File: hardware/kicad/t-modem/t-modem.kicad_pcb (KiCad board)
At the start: 2 copper layers, 190 x 110 mm, 43 parts, among them Q1 2N2222A, SW1 BOOTSEL, U1 RaspberryPi_Pico, Y1 4.433619

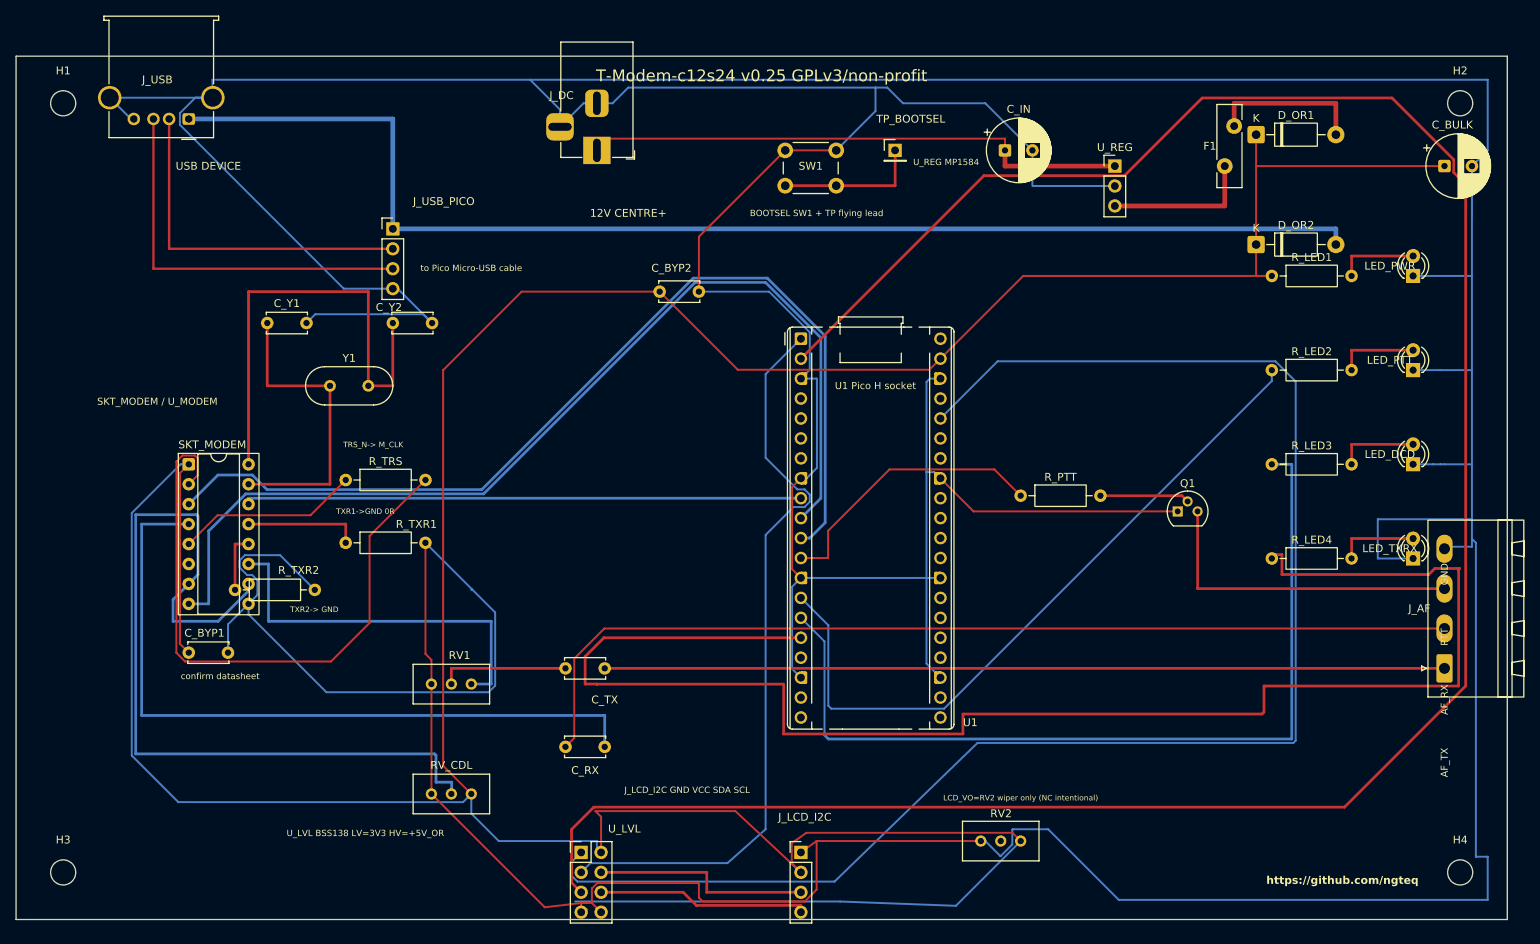
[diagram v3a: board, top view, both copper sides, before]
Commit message: fix(pcb): polish edge placement for prototype-ready layout
Nudge silkscreen/refdes and connector positions off the board edge so the
c12s24 PCB reads as fabrication-ready without further edge cleanup.

Co-authored-by: Cursor <cursoragent@cursor.com>
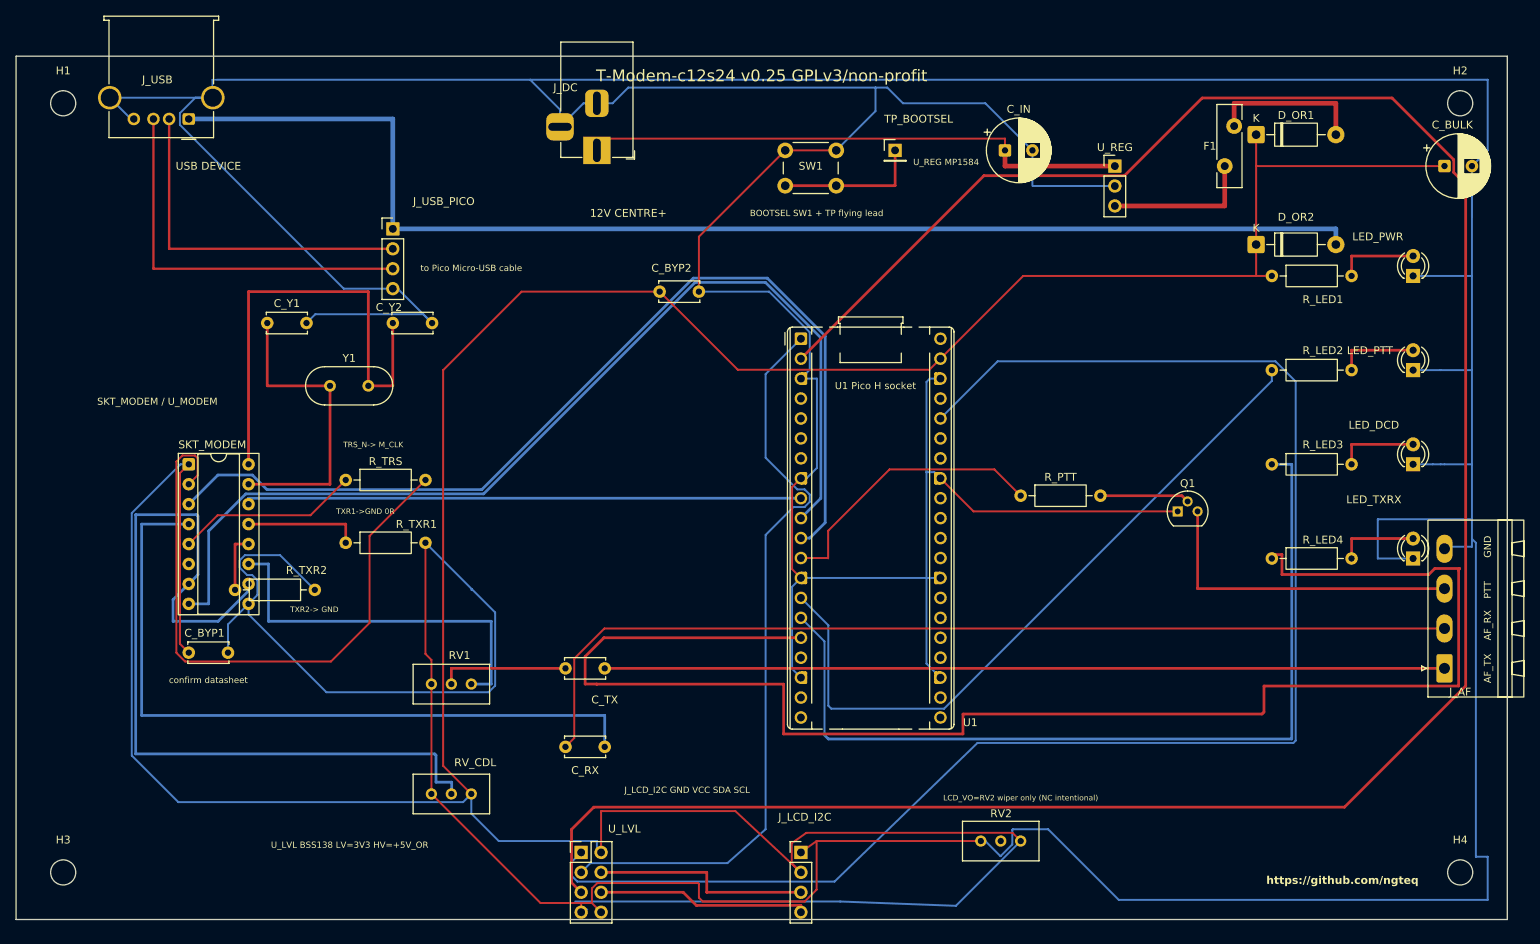
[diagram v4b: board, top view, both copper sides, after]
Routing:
- net GND: track 977.0 -> 978.1 mm
- net +5V_OR: track 499.4 -> 498.4 mm
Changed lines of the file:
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@@
 		(tags "Through hole pin header THT 1x01 2.54mm single row")
 		(property "Reference" "TP_BOOTSEL"
-			(at 2 -4 0)
+			(at 3 -4 0)
 			(layer "F.SilkS")
 			(effects
@@
 		(tags "phoenix_contact connector MSTBA_01x04_G_5.08mm")
 		(property "Reference" "J_AF"
-			(at 7.62 -3.2 0)
+			(at -3 2 0)
 			(layer "F.SilkS")
 			(effects
@@
 		(tags "Power Jack")
 		(property "Reference" "J_DC"
-			(at -7 4.5 0)
+			(at -8 4 0)
 			(layer "F.SilkS")
 			(effects
@@
 		(tags "Resistor Axial_DIN0207 series Axial Horizontal pin pitch 10.16mm 0.25W = 1/4W length 6.3mm diameter 2.5mm")
 		(property "Reference" "R_LED2"
-			(at 5.08 -2.37 0)
+			(at 6.5 -2.5 0)
 			(layer "F.SilkS")
 			(effects
@@
 		(tags "Potentiometer vertical Bourns 3296W")
 		(property "Reference" "RV_CDL"
-			(at -2.54 -3.66 0)
+			(at 0.5 -4 0)
 			(layer "F.SilkS")
 			(effects
@@
 		(tags "LED")
 		(property "Reference" "LED_TXRX"
-			(at 1.27 -2.96 0)
+			(at 7.5 -5 0)
 			(layer "F.SilkS")
 			(effects
@@
 		(tags "Resistor Axial_DIN0207 series Axial Horizontal pin pitch 10.16mm 0.25W = 1/4W length 6.3mm diameter 2.5mm")
 		(property "Reference" "R_LED1"
-			(at 5.08 -2.37 0)
+			(at 6.5 3 0)
 			(layer "F.SilkS")
 			(effects
@@
 		(tags "LED")
 		(property "Reference" "LED_PWR"
-			(at 1.27 -2.96 0)
+			(at 5 -4.5 0)
 			(layer "F.SilkS")
 			(effects
@@
 		(tags "Diode DO-41_SOD81 series Axial Horizontal pin pitch 10.16mm  length 5.2mm diameter 2.7mm")
 		(property "Reference" "D_OR2"
-			(at 5.08 -2.47 0)
+			(at 5.08 -3.5 0)
 			(layer "F.SilkS")
 			(effects
@@
 		(tags "Resistor Axial_DIN0207 series Axial Horizontal pin pitch 10.16mm 0.25W = 1/4W length 6.3mm diameter 2.5mm")
 		(property "Reference" "R_TXR2"
-			(at 8.1 -2.5 0)
+			(at 9.1 -2.5 0)
 			(layer "F.SilkS")
 			(effects
@@
 		(tags "Resistor Axial_DIN0207 series Axial Horizontal pin pitch 10.16mm 0.25W = 1/4W length 6.3mm diameter 2.5mm")
 		(property "Reference" "R_LED4"
-			(at 5.08 -2.37 0)
+			(at 6.5 -2.37 0)
 			(layer "F.SilkS")
 			(effects
@@
 		(tags "LED")
 		(property "Reference" "LED_DCD"
-			(at 1.27 -2.96 0)
+			(at 5 -5 0)
 			(layer "F.SilkS")
 			(effects
@@
 		(tags "Resistor Axial_DIN0207 series Axial Horizontal pin pitch 10.16mm 0.25W = 1/4W length 6.3mm diameter 2.5mm")
 		(property "Reference" "R_LED3"
-			(at 5.08 -2.37 0)
+			(at 6.5 -2.5 0)
 			(layer "F.SilkS")
 			(effects
@@
 		(tags "LED")
 		(property "Reference" "LED_PTT"
-			(at 1.27 -2.96 0)
+			(at 2.5 -5.5 0)
 			(layer "F.SilkS")
 			(effects
@@
 	)
 	(gr_text "confirm datasheet"
-		(at 26 79 0)
+		(at 24.5 79.5 0)
 		(layer "F.SilkS")
 		(effects
@@
 	)
 	(gr_text "U_LVL BSS138 LV=3V3 HV=+5V_OR"
-		(at 44.5 99 0)
+		(at 42.5 100.5 0)
 		(layer "F.SilkS")
 		(effects
@@
 	)
 	(gr_text "GND"
-		(at 182 66 90)
+		(at 187.5 62.5 90)
 		(layer "F.SilkS")
 		(effects
@@
 	)
 	(gr_text "PTT"
-		(at 182 74 90)
+		(at 187.5 68 90)
 		(layer "F.SilkS")
 		(effects
@@
 	)
 	(gr_text "AF_RX"
-		(at 182 82 90)
+		(at 187.5 72.5 90)
 		(layer "F.SilkS")
 		(effects
@@
 	)
 	(gr_text "AF_TX"
-		(at 182 90 90)
+		(at 187.5 78 90)
 		(layer "F.SilkS")
 		(effects
@@
 	)
 	(segment
-		(start 67.365 108.445)
-		(end 72 107.895)
-		(width 0.25)
-		(layer "F.Cu")
-		(net "GND")
-	)
-	(segment
 		(start 52.92 94)
 		(end 52.92 80)
@@
 	)
 	(segment
+		(start 52.92 94)
+		(end 66.815 107.895)
+		(width 0.25)
+		(layer "F.Cu")
+		(net "GND")
+	)
+	(segment
 		(start 72 107.895)
 		(end 73.365 107.895)
@@
 	)
 	(segment
-		(start 52.92 94)
-		(end 67.365 108.445)
-		(width 0.25)
-		(layer "F.Cu")
-		(net "GND")
-	)
-	(segment
 		(start 87 30)
 		(end 87 23)
@@
 		(net "GND")
 	)
+	(segment
+		(start 73.365 107.895)
+		(end 66.815 107.895)
+		(width 0.25)
+		(layer "F.Cu")
+		(net "GND")
+	)
 	(via
 		(at 100 53.78)
@@
 	)
 	(segment
+		(start 74.54 96.225)
+		(end 74.54 101.45)
+		(width 0.25)
+		(layer "F.Cu")
+		(net "+5V_OR")
+	)
+	(segment
 		(start 98.825 102.815)
 		(end 98.825 100.275)
@@
 	)
 	(segment
-		(start 74.54 96.91)
-		(end 74.54 101.45)
+		(start 74.58 96.185)
+		(end 74.54 96.225)
 		(width 0.25)
 		(layer "F.Cu")
@@
 	)
 	(segment
-		(start 73.815 96.185)
-		(end 74.54 96.91)
+		(start 20.875 53.125)
+		(end 20.875 74.875)
 		(width 0.25)
 		(layer "F.Cu")
@@
 	)
 	(segment
-		(start 20.875 53.125)
-		(end 20.875 74.875)
+		(start 91.645 96.185)
+		(end 74.58 96.185)
 		(width 0.25)
 		(layer "F.Cu")
@@
 	)
 	(segment
-		(start 91.645 96.185)
-		(end 73.815 96.185)
-		(width 0.25)
-		(layer "F.Cu")
-		(net "+5V_OR")
-	)
-	(segment
 		(start 158 14)
 		(end 158 24)
@@
 	)
 	(segment
-		(start 71.236767 107.705)
-		(end 105 107.705)
-		(width 0.25)
-		(layer "B.Cu")
-		(net "+5V_OR")
-	)
-	(segment
-		(start 105 107.705)
-		(end 119.745 108.255)
-		(width 0.25)
-		(layer "B.Cu")
-		(net "+5V_OR")
-	)
-	(segment
 		(start 61.5 100)
 		(end 74 100)
@@
 	)
 	(segment
+		(start 71.236767 107.705)
+		(end 105 107.705)
+		(width 0.25)
+		(layer "B.Cu")
+		(net "+5V_OR")
+	)
+	(segment
 		(start 14.74 89.107107)
 		(end 14.74 58.212893)
@@
 	)
 	(segment
+		(start 105 107.705)
+		(end 119.745 108.255)
+		(width 0.25)
+		(layer "B.Cu")
+		(net "+5V_OR")
+	)
+	(segment
 		(start 58 94)
 		(end 56.955 95.045)
@@
 		(net "+5V_OR")
 	)
+	(segment
+		(start 20.425 51.6549)
+		(end 21.2049 50.875)
+		(width 0.25)
+		(layer "F.Cu")
+		(net "MODEM_CLK")
+	)
+	(segment
+		(start 21.2049 50.875)
+		(end 22.7951 50.875)
+		(width 0.25)
+		(layer "F.Cu")
+		(net "MODEM_CLK")
+	)
+	(segment
+		(start 40.122107 77.125)
+		(end 21.534009 77.125)
+		(width 0.25)
+		(layer "F.Cu")
+		(net "MODEM_CLK")
+	)
+	(segment
+		(start 52.16 54)
+		(end 45.04 61.12)
+		(width 0.25)
+		(layer "F.Cu")
+		(net "MODEM_CLK")
+	)
+	(segment
+		(start 22.7951 50.875)
+		(end 23.125 51.2049)
+		(width 0.25)
+		(layer "F.Cu")
+		(net "MODEM_CLK")
+	)
+	(segment
+		(start 23.125 51.2049)
+		(end 23.125 53.415)
+		(width 0.25)
+		(layer "F.Cu")
+		(net "MODEM_CLK")
+	)
+	(segment
+		(start 45.04 72.207107)
+		(end 40.122107 77.125)
+		(width 0.25)
+		(layer "F.Cu")
+		(net "MODEM_CLK")
+	)
+	(segment
+		(start 21.534009 77.125)
+		(end 20.425 76.015991)
+		(width 0.25)
+		(layer "F.Cu")
+		(net "MODEM_CLK")
+	)
+	(segment
+		(start 20.425 76.015991)
+		(end 20.425 51.6549)
+		(width 0.25)
+		(layer "F.Cu")
+		(net "MODEM_CLK")
+	)
+	(segment
+		(start 45.04 61.12)
+		(end 45.04 72.207107)
+		(width 0.25)
+		(layer "F.Cu")
+		(net "MODEM_CLK")
+	)
+	(segment
+		(start 23.125 53.415)
+		(end 22 54.54)
+		(width 0.25)
+		(layer "F.Cu")
+		(net "MODEM_CLK")
+	)
 	(via
 		(at 100 61.4)
@@
 		(net "LED_DCD_A")
 	)
-	(segment
-		(start 20.425 51.6549)
-		(end 21.2049 50.875)
-		(width 0.25)
-		(layer "F.Cu")
-		(net "MODEM_CLK")
-	)
-	(segment
-		(start 21.2049 50.875)
-		(end 22.7951 50.875)
-		(width 0.25)
-		(layer "F.Cu")
-		(net "MODEM_CLK")
-	)
-	(segment
-		(start 40.122107 77.125)
-		(end 21.534009 77.125)
-		(width 0.25)
-		(layer "F.Cu")
-		(net "MODEM_CLK")
-	)
-	(segment
-		(start 52.16 54)
-		(end 45.04 61.12)
-		(width 0.25)
-		(layer "F.Cu")
-		(net "MODEM_CLK")
-	)
-	(segment
-		(start 22.7951 50.875)
-		(end 23.125 51.2049)
-		(width 0.25)
-		(layer "F.Cu")
-		(net "MODEM_CLK")
-	)
-	(segment
-		(start 23.125 51.2049)
-		(end 23.125 53.415)
-		(width 0.25)
-		(layer "F.Cu")
-		(net "MODEM_CLK")
-	)
-	(segment
-		(start 45.04 72.207107)
-		(end 40.122107 77.125)
-		(width 0.25)
-		(layer "F.Cu")
-		(net "MODEM_CLK")
-	)
-	(segment
-		(start 21.534009 77.125)
-		(end 20.425 76.015991)
-		(width 0.25)
-		(layer "F.Cu")
-		(net "MODEM_CLK")
-	)
-	(segment
-		(start 20.425 76.015991)
-		(end 20.425 51.6549)
-		(width 0.25)
-		(layer "F.Cu")
-		(net "MODEM_CLK")
-	)
-	(segment
-		(start 45.04 61.12)
-		(end 45.04 72.207107)
-		(width 0.25)
-		(layer "F.Cu")
-		(net "MODEM_CLK")
-	)
-	(segment
-		(start 23.125 53.415)
-		(end 22 54.54)
-		(width 0.25)
-		(layer "F.Cu")
-		(net "MODEM_CLK")
-	)
 	(embedded_fonts no)
